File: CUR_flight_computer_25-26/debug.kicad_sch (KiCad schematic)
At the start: 8 parts, among them J1 3220-14-0100-00, J15 FTSH-107-01-X-DV-K-TR

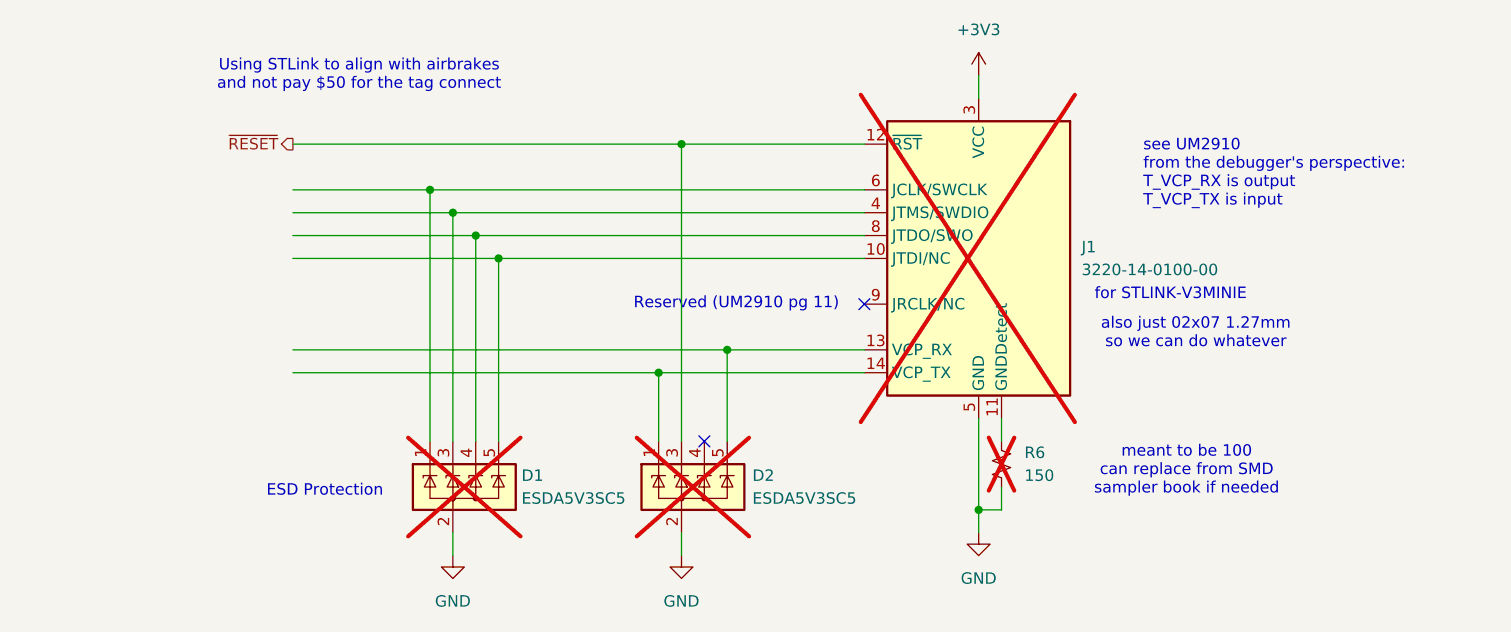
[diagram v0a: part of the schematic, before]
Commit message: Remove other debug connector for clarity
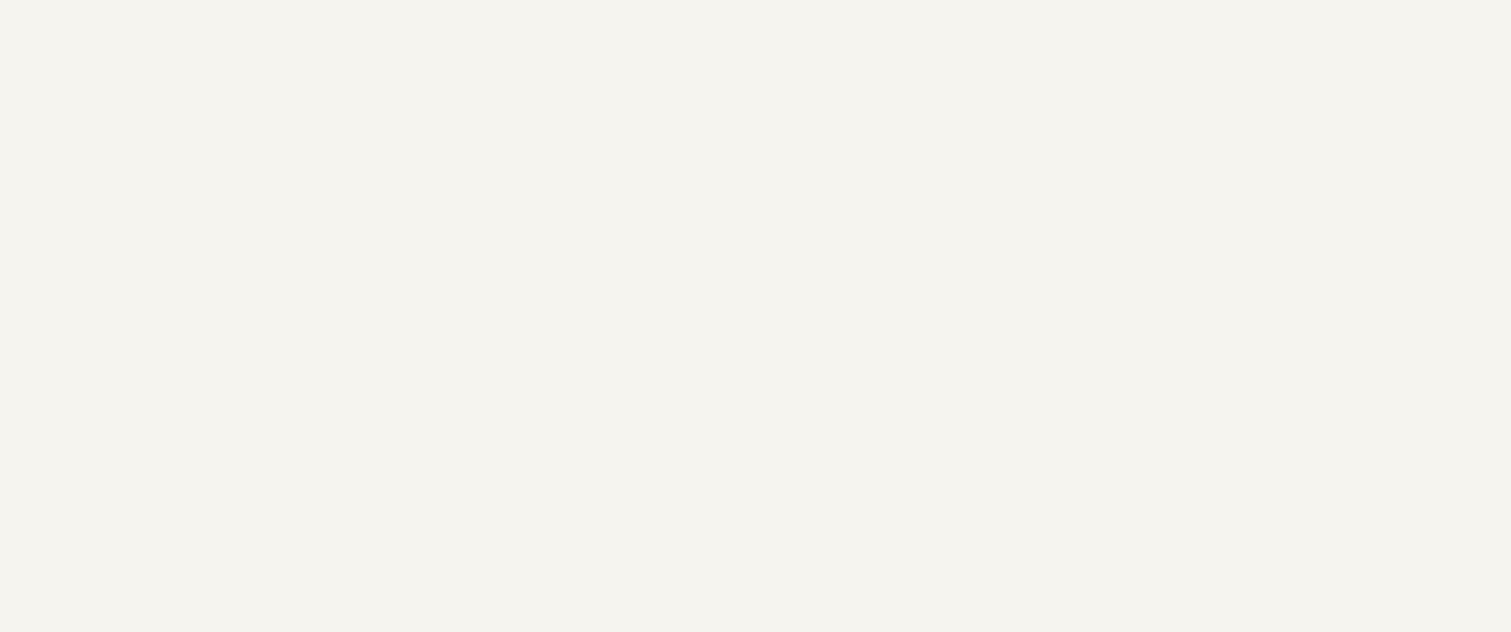
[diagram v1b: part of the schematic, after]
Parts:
- removed D1, D2: ESDA5V3SC5, Package_TO_SOT_SMD:SOT-23-5, symbol Power_Protection:ESDA5V3SC5
- removed J1: 3220-14-0100-00, Connector_SAMTEC_FTSH-107-01-X-DV-K-TR:SAMTEC_FTSH-107-01-X-DV-K-TR, symbol Connector:Conn_ST_STDC14
- removed R6: 150, Resistor_SMD:R_0603_1608Metric, symbol Device:R_Small_US
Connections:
- no-connect marks 9 -> 7
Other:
- note removed: "Reserved (UM2910 pg 11)"
- note removed: "Using STLink to align with airbrakes and not pay $50 for the tag connect"
- note removed: "also just 02x07 1.27mm so we can do whatever"
- note removed: "for STLINK-V3MINIE"
- note removed: "meant to be 100 can replace from SMD sampler book if needed"
- note removed: "see UM2910 from the debugger's perspective: T_VCP_RX is output T_VCP_TX is input"

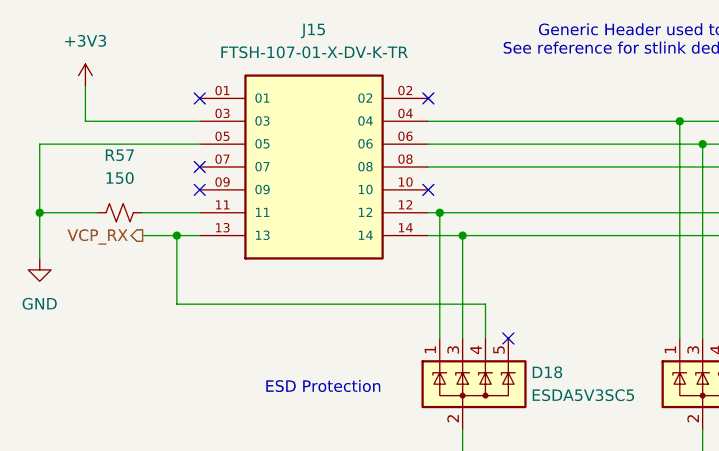
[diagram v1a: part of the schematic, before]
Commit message: Add MPNs for ICs
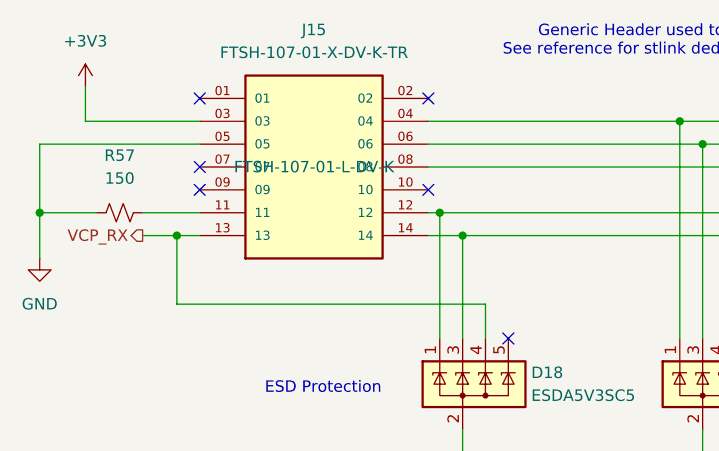
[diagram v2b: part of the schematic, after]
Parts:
- J15: MPN (none) -> FTSH-107-01-L-DV-K
- R57: MPN RC0603JR-07150RL -> RC0603FR-07150RL
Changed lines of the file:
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@@
+			)
+		)
+		(property "MPN" "FTSH-107-01-L-DV-K"
+			(at 53.34 40.64 0)
+			(effects
+				(font
+					(size 1.27 1.27)
+				)
 			)
 		)
@@
 			)
 		)
-		(property "MPN" "RC0603JR-07150RL"
+		(property "MPN" "RC0603FR-07150RL"
 			(at 31.75 45.72 0)
 			(effects

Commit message: Hide MPNs
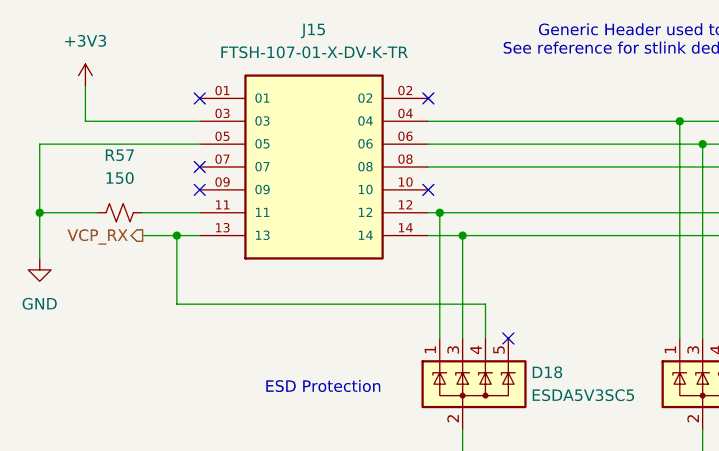
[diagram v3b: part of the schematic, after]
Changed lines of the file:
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@@
 					(size 1.27 1.27)
 				)
+				(hide yes)
 			)
 		)

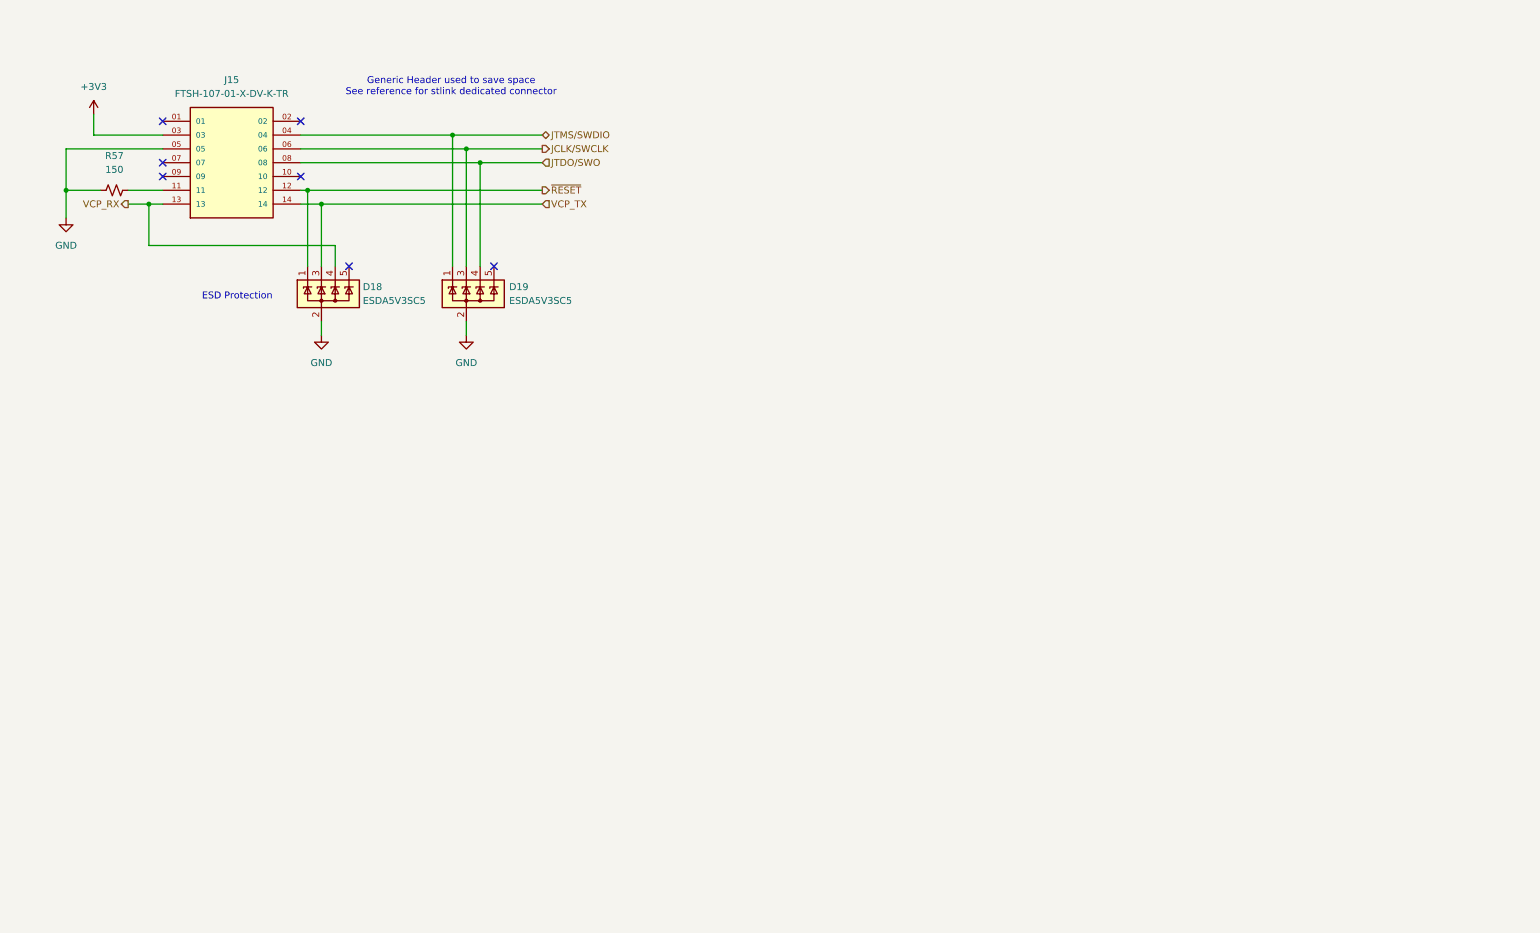
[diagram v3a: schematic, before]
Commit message: Cleaned up schematic
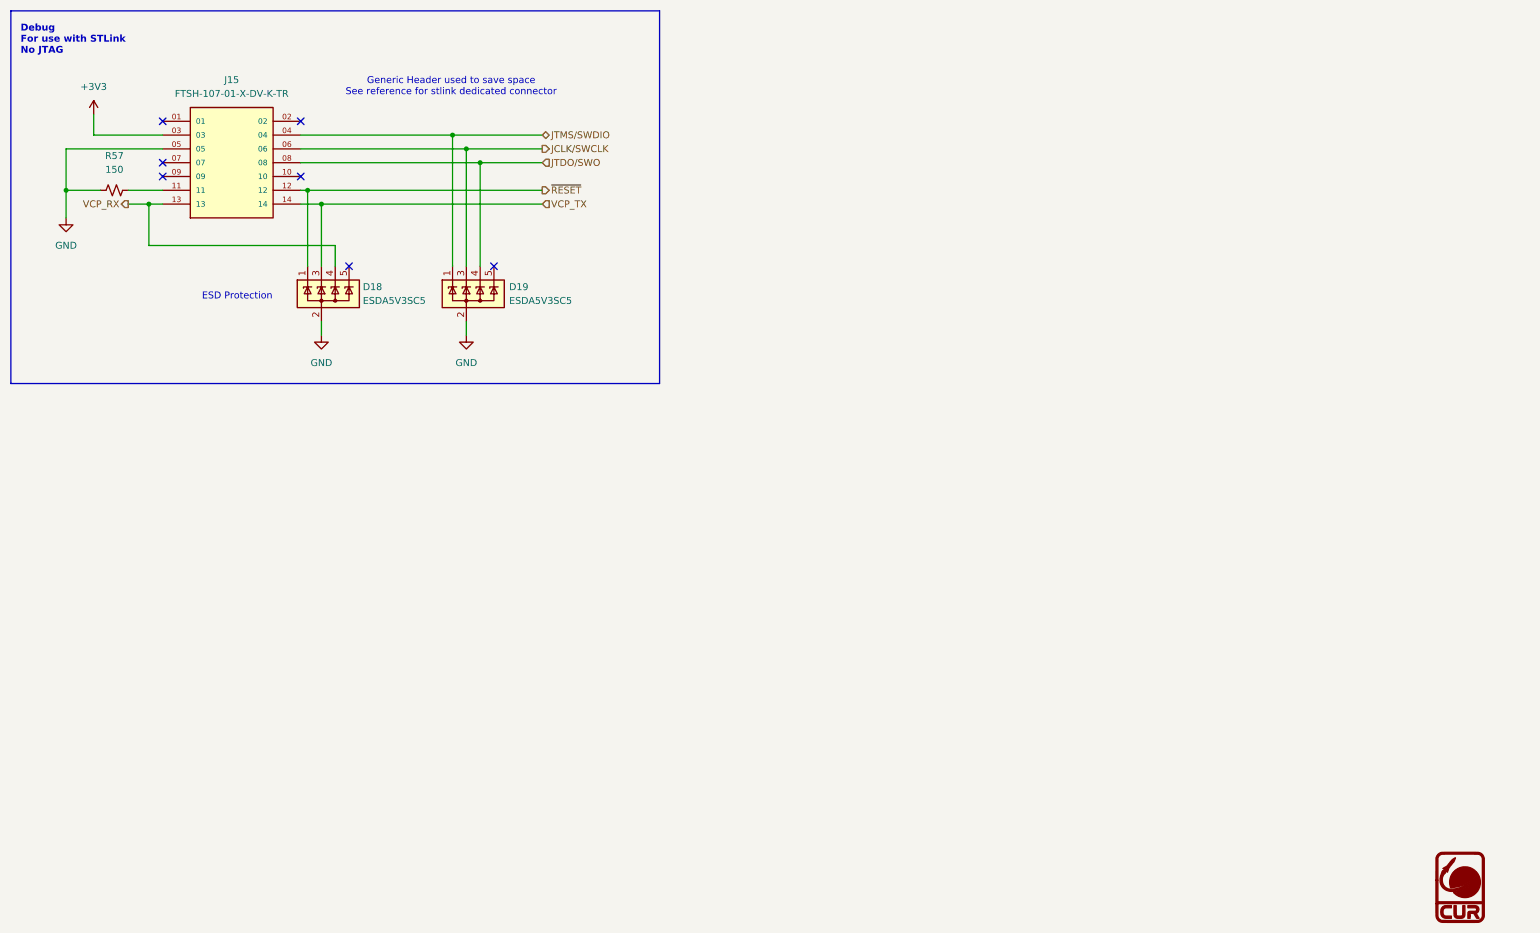
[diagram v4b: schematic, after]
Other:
- note added: "Debug For use with STLink No JTAG"
- company: (none) -> Clarkson University Rocketry
- title: (none) -> Flight Computer
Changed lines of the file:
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@@
 	(generator_version "9.0")
 	(paper "A4")
+	(title_block
+		(title "Flight Computer")
+		(date "2026-03-18")
+		(company "Clarkson University Rocketry")
+	)
+	(rectangle
+		(start 12.7 12.7)
+		(end 132.08 81.28)
+		(stroke
+			(width 0)
+			(type default)
+		)
+		(fill
+			(type none)
+		)
+	)
 	(text "ESD Protection"
 		(exclude_from_sim no)
@@
 				(size 1.27 1.27)
 			)
+		)
+	)
+	(text "Debug\nFor use with STLink\nNo JTAG"
+		(exclude_from_sim no)
+		(at 14.478 18.034 0)
+		(effects
+			(font
+				(size 1.27 1.27)
+				(thickness 0.254)
+				(bold yes)
+			)
+			(justify left)
 		)
 	)
@@
 					(unit 1)
 				)
+			)
+		)
+	)
+	(symbol
+		(lib_id "CUR_Logo:LOGO")
+		(at 279.4 173.99 0)
+		(unit 1)
+		(exclude_from_sim no)
+		(in_bom yes)
+		(on_board yes)
+		(dnp no)
+		(fields_autoplaced yes)
+		(property "Reference" "#G4"
+			(at 279.4 167.002 0)
+			(effects
+				(font
+					(size 1.27 1.27)
+				)
+				(hide yes)
+			)
+		)
+		(property "Value" "LOGO"
+			(at 279.4 180.978 0)
+			(effects
+				(font
+					(size 1.27 1.27)
+				)
+				(hide yes)
+			)
+		)
+		(property "Footprint" ""
+			(at 279.4 173.99 0)
+			(effects
+				(font
+					(size 1.27 1.27)
+				)
+				(hide yes)
+			)
+		)
+		(property "Datasheet" ""
+			(at 279.4 173.99 0)
+			(effects
+				(font
+					(size 1.27 1.27)
+				)
+				(hide yes)
+			)
+		)
+		(property "Description" ""
+			(at 279.4 173.99 0)
+			(effects
+				(font
+					(size 1.27 1.27)
+				)
+				(hide yes)
+			)
+		)
+		(instances
+			(project "CUR_flight_computer_25-26"
+				(path "/bf7761cc-1b32-4d86-809c-5f027005229b/0389a778-0ae1-4921-8e0e-3c33d2286cb8"
+					(reference "#G4")
+					(unit 1)
+				)

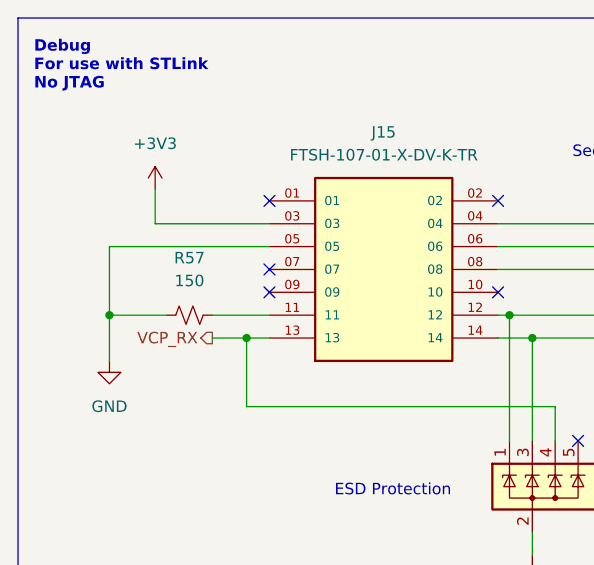
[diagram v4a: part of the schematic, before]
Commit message: BOM optimize resistors
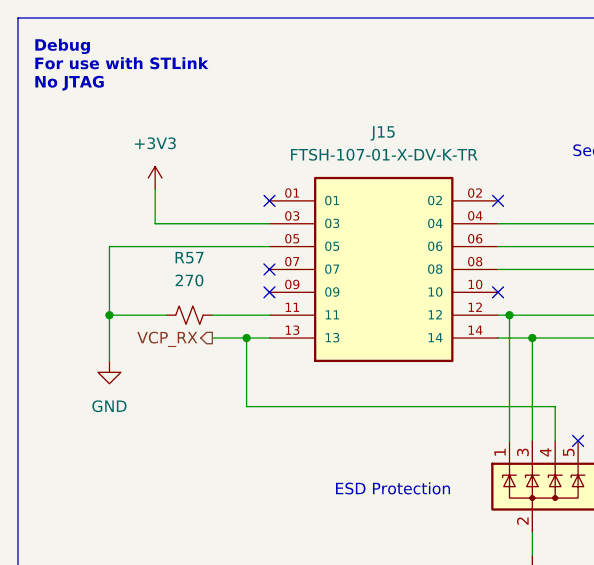
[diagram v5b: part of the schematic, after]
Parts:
- R57: value 150 -> 270
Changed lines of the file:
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@@
 			)
 		)
-		(property "Value" "150"
+		(property "Value" "270"
 			(at 31.75 41.91 90)
 			(effects

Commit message: Apply resistor MPNs
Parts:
- R57: MPN RC0603FR-07150RL -> RC0603JR-07270RL
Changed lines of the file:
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@@
 			)
 		)
-		(property "MPN" "RC0603FR-07150RL"
+		(property "MPN" "RC0603JR-07270RL"
 			(at 31.75 45.72 0)
 			(effects
